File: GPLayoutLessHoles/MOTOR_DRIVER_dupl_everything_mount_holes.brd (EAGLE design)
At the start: 340.4 x 63 mm, 196 parts, among them T1 2N2222, T2 2N2222, T3 2N2222, T4 2N2222, U1 ATMEGA328P_TQFP, U7 ATMEGA328P_TQFP, Y1 16MHz, Y2 16MHz

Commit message: added more mounting holes and headers, renamed switches. ordered this 3/20
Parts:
- added H10, H11, H12, H13, H14, H15, H16, H9: MOUNT-HOLE3.3, holes:3,3
- added SV19, SV20: (no value), con-lsta:FE04-1
- moved SV16 4.50 mm to (315.0, 22.6)
- moved SV9 4.00 mm to (144.5, 22.6)
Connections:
- new net THERM1: LED1.THERMAL
- new net THERM1_DUP: LED3.THERMAL
- new net THERM2: LED2.THERMAL
- new net THERM2_DUP: LED4.THERMAL
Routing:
- net GND_TOP2: track 54.0 -> 50.3 mm
- net GND_TOP2_DUP: track 54.0 -> 50.9 mm
- net 7_4V_TOP2: track 71.2 -> 68.2 mm
- net 7_4V_TOP2_DUP: track 71.2 -> 68.3 mm
- net LED2HI_DUP: track 14.0 -> 12.7 mm
- net LED2HI: track 14.0 -> 12.7 mm
- net LED1LO_DUP: track 13.4 -> 12.2 mm
- net LED1HI_DUP: track 13.0 -> 11.9 mm
- net LED2LO_DUP: track 13.2 -> 12.1 mm
- net LED2LO: track 13.2 -> 12.1 mm
- net LED1HI: track 13.0 -> 12.0 mm
- net LED1LO: track 13.4 -> 12.4 mm
- net N$19: track 20.4 -> 19.5 mm
- net N$45: track 20.4 -> 19.5 mm
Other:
- board text added: "SENSE"
- board text added: "SW1"
- board text added: "SW2"
- board text added: "SW3"
- board text added: "SW4"

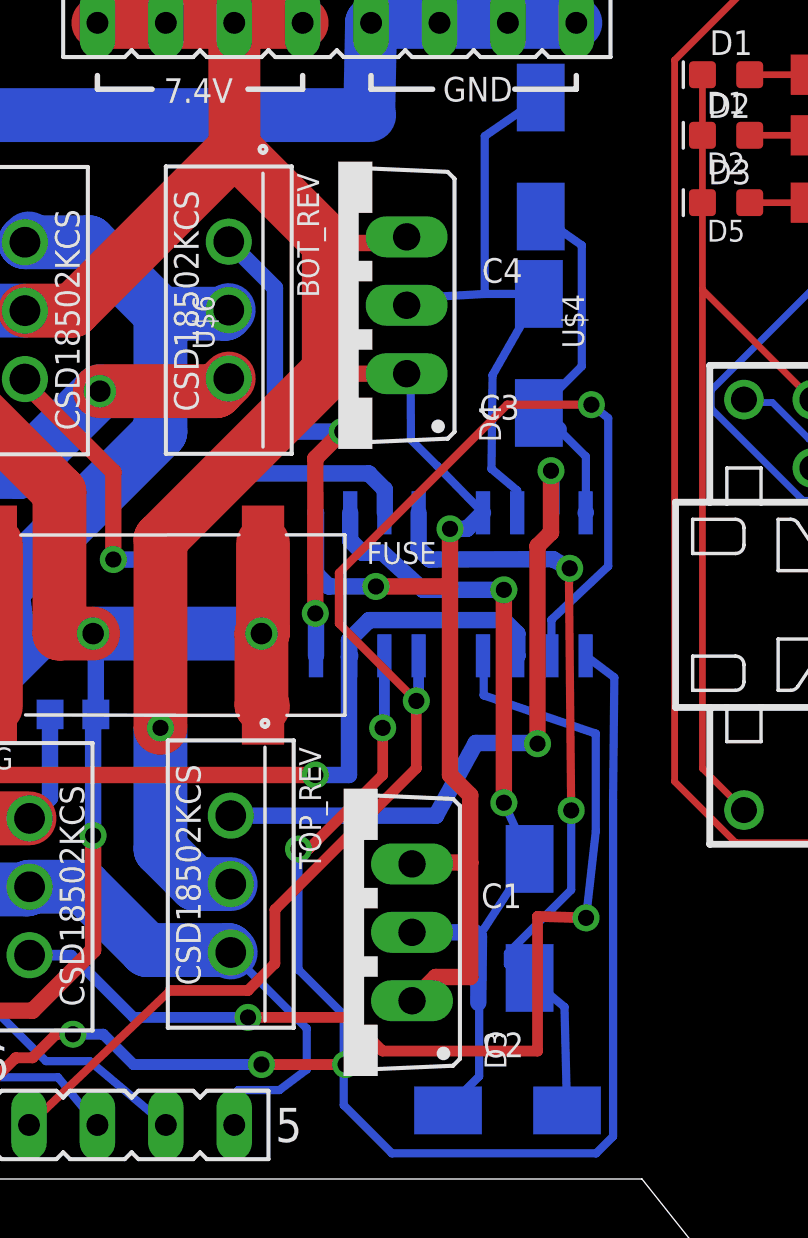
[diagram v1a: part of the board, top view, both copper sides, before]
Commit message: some modified board and new driving code for single thread and half or full bridge
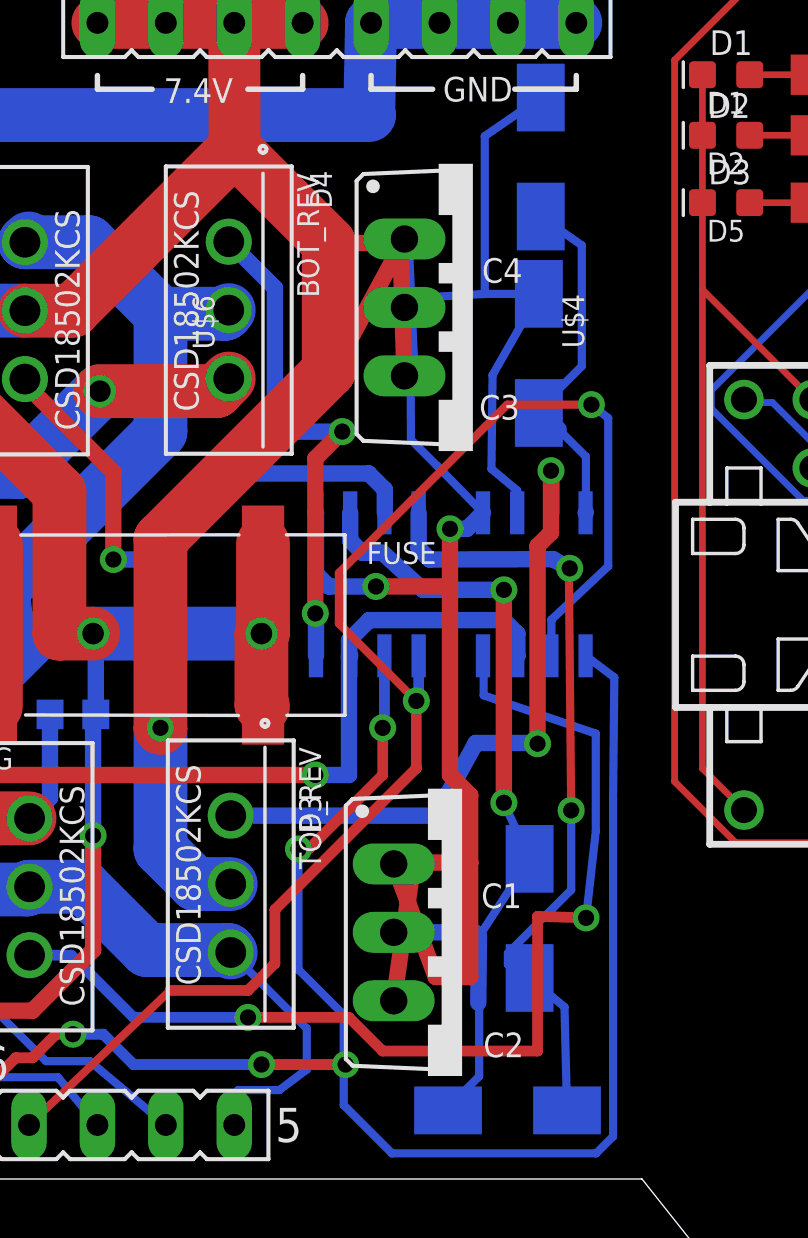
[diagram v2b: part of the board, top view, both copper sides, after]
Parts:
- R17, R35: value 10m -> 20m
- R18, R36: value 10k -> 100k
- moved D4 5.00 mm to (33.6, 32.4), turned to 270 degrees
- moved D3 4.40 mm to (33.2, 9.16), turned to 270 degrees
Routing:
- net 7_4V_TOP: track 136.8 -> 157.6 mm
- net N$5: track 30.6 -> 31.3 mm
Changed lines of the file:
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@@
 <setting verticaltext="up"/>
 </settings>
-<grid distance="0.5" unitdist="mm" unit="mm" style="lines" multiple="1" display="yes" altdistance="0.25" altunitdist="mm" altunit="mm"/>
+<grid distance="0.1" unitdist="mm" unit="mm" style="lines" multiple="1" display="yes" altdistance="0.01" altunitdist="mm" altunit="mm"/>
 <layers>
-<layer number="1" name="Top" color="4" fill="1" visible="yes" active="yes"/>
+<layer number="1" name="Top" color="4" fill="1" visible="no" active="yes"/>
 <layer number="2" name="Route2" color="1" fill="3" visible="no" active="no"/>
 <layer number="3" name="Route3" color="4" fill="3" visible="no" active="no"/>
@@
 <layer number="14" name="Route14" color="1" fill="6" visible="no" active="no"/>
 <layer number="15" name="Route15" color="4" fill="6" visible="no" active="no"/>
-<layer number="16" name="Bottom" color="1" fill="1" visible="yes" active="yes"/>
+<layer number="16" name="Bottom" color="1" fill="1" visible="no" active="yes"/>
 <layer number="17" name="Pads" color="2" fill="1" visible="yes" active="yes"/>
 <layer number="18" name="Vias" color="2" fill="1" visible="yes" active="yes"/>
@@
 <attribute name="VALUE" x="109.3604" y="15.437" size="0.8128" layer="27" ratio="10" rot="R180"/>
 </element>
-<element name="D3" library="diode" package="TO220ABS" value="BYV32" x="28.8" y="9.158" smashed="yes" rot="R90">
-<attribute name="NAME" x="34.8452" y="4.078" size="0.8128" layer="25" ratio="10" rot="R90"/>
-<attribute name="VALUE" x="36.42" y="4.078" size="0.8128" layer="27" ratio="10" rot="R90"/>
-</element>
-<element name="D4" library="diode" package="TO220ABS" value="BYV32" x="28.6" y="32.44" smashed="yes" rot="R90">
-<attribute name="NAME" x="34.6452" y="27.36" size="0.8128" layer="25" ratio="10" rot="R90"/>
-<attribute name="VALUE" x="36.22" y="27.36" size="0.8128" layer="27" ratio="10" rot="R90"/>
+<element name="D3" library="diode" package="TO220ABS" value="BYV32" x="33.2" y="9.158" smashed="yes" rot="R270">
+<attribute name="NAME" x="27.1548" y="14.238" size="0.8128" layer="25" ratio="10" rot="R270"/>
+<attribute name="VALUE" x="25.58" y="14.238" size="0.8128" layer="27" ratio="10" rot="R270"/>
+</element>
+<element name="D4" library="diode" package="TO220ABS" value="BYV32" x="33.6" y="32.36" smashed="yes" rot="R270">
+<attribute name="NAME" x="27.5548" y="37.44" size="0.8128" layer="25" ratio="10" rot="R270"/>
+<attribute name="VALUE" x="25.98" y="37.44" size="0.8128" layer="27" ratio="10" rot="R270"/>
 </element>
 <element name="MOTOR_POS" library="solpad" package="SE14" value="SE14" x="3.51" y="13.61" smashed="yes">
@@
 <attribute name="VALUE" x="70.7873" y="6.0282" size="1.27" layer="27" ratio="10"/>
 </element>
-<element name="R17" library="rcl" package="R2512" value="10m" x="14.394540625" y="18.11175" smashed="yes" rot="MR315">
+<element name="R17" library="rcl" package="R2512" value="20m" x="14.394540625" y="18.11175" smashed="yes" rot="MR315">
 <attribute name="NAME" x="14.84355625" y="21.2548375" size="0.8128" layer="26" rot="MR315"/>
 <attribute name="VALUE" x="18.43565625" y="17.662734375" size="0.8128" layer="28" rot="MR315"/>
@@
 <attribute name="VALUE" x="4.528" y="14.202" size="0.8128" layer="28" ratio="10" rot="MR0"/>
 </element>
-<element name="R18" library="rcl" package="R0603" value="10k" x="6.875" y="20.5" smashed="yes" rot="MR0">
+<element name="R18" library="rcl" package="R0603" value="100k" x="6.875" y="20.5" smashed="yes" rot="MR0">
 <attribute name="NAME" x="7.51" y="21.135" size="0.8128" layer="26" rot="MR0"/>
 <attribute name="VALUE" x="7.51" y="18.595" size="0.8128" layer="28" rot="MR0"/>
@@
 <attribute name="VALUE" x="240.7873" y="6.0282" size="1.27" layer="27" ratio="10"/>
 </element>
-<element name="R35" library="rcl" package="R2512" value="10m" x="184.394540625" y="18.11175" smashed="yes" rot="MR315">
+<element name="R35" library="rcl" package="R2512" value="20m" x="184.394540625" y="18.11175" smashed="yes" rot="MR315">
 <attribute name="NAME" x="184.84355625" y="21.2548375" size="0.8128" layer="26" rot="MR315"/>
 <attribute name="VALUE" x="188.43565625" y="17.662734375" size="0.8128" layer="28" rot="MR315"/>
@@
 <attribute name="VALUE" x="174.528" y="14.202" size="0.8128" layer="28" ratio="10" rot="MR0"/>
 </element>
-<element name="R36" library="rcl" package="R0603" value="10k" x="176.875" y="20.5" smashed="yes" rot="MR0">
+<element name="R36" library="rcl" package="R0603" value="100k" x="176.875" y="20.5" smashed="yes" rot="MR0">
 <attribute name="NAME" x="177.51" y="21.135" size="0.8128" layer="26" rot="MR0"/>
 <attribute name="VALUE" x="177.51" y="18.595" size="0.8128" layer="28" rot="MR0"/>
@@
 <wire x1="34.75" y1="21.875" x2="34.75" y2="13.97" width="0.6096" layer="1"/>
 <wire x1="34.75" y1="13.97" x2="35.7052" y2="11.8838" width="0.3048" layer="16"/>
-<wire x1="31.34" y1="9.158" x2="33.6676" y2="9.158" width="0.6096" layer="16"/>
+<wire x1="30.66" y1="9.158" x2="33.6676" y2="9.158" width="0.6096" layer="16"/>
 <wire x1="33.6676" y1="9.158" x2="33.8256" y2="9" width="0.6096" layer="16"/>
 <wire x1="31.75" y1="21.875" x2="30.25" y2="23.25" width="0.6096" layer="16"/>
@@
 <wire x1="34.04" y1="38.72" x2="36.12" y2="40.1522" width="0.3048" layer="16"/>
 <wire x1="34.04" y1="32.8596" x2="31.33" y2="32.7072" width="0.3048" layer="16"/>
-<wire x1="31.33" y1="32.7072" x2="31.14" y2="32.44" width="0.6096" layer="16"/>
+<wire x1="31.33" y1="32.7072" x2="31.06" y2="32.36" width="0.6096" layer="16"/>
 <wire x1="35.245" y1="24.7343" x2="35.245" y2="25.5626" width="0.3048" layer="16"/>
 <wire x1="35.245" y1="25.5626" x2="34.29" y2="26.3652" width="0.3048" layer="16"/>
@@
 <wire x1="32.275" y1="26.475" x2="31.3" y2="27.45" width="0.3048" layer="16"/>
 <wire x1="31.3" y1="27.45" x2="31.29" y2="29.75" width="0.3048" layer="16"/>
-<wire x1="31.29" y1="29.75" x2="31.14" y2="29.9" width="0.6096" layer="16"/>
+<wire x1="31.29" y1="29.75" x2="31.06" y2="34.9" width="0.6096" layer="16"/>
 <wire x1="27.75" y1="24.7593" x2="27.775" y2="24.7343" width="0.6096" layer="16"/>
 <via x="32.75" y="24.1404" extent="1-16" drill="0.6"/>
@@
 <wire x1="22" y1="12.25" x2="22" y2="16.75" width="2" layer="16"/>
 <wire x1="28.25" y1="34.75" x2="30.91" y2="34.75" width="0.6096" layer="1"/>
-<wire x1="30.91" y1="34.75" x2="31.14" y2="34.98" width="0.6096" layer="1"/>
-<wire x1="31.14" y1="29.9" x2="28.35" y2="29.9" width="0.6096" layer="1"/>
+<wire x1="30.91" y1="34.75" x2="31.06" y2="29.82" width="0.6096" layer="1"/>
+<wire x1="31.06" y1="34.9" x2="28.35" y2="29.9" width="0.6096" layer="1"/>
 <wire x1="28.35" y1="29.9" x2="28.25" y2="30" width="0.6096" layer="1"/>
 <wire x1="33.5" y1="11.75" x2="31.392" y2="11.75" width="0.6096" layer="1"/>
-<wire x1="31.392" y1="11.75" x2="31.34" y2="11.698" width="0.6096" layer="1"/>
+<wire x1="31.392" y1="11.75" x2="30.66" y2="6.618" width="0.6096" layer="1"/>
 <wire x1="33.5" y1="7.5" x2="32.222" y2="7.5" width="0.6096" layer="1"/>
-<wire x1="32.222" y1="7.5" x2="31.34" y2="6.618" width="0.6096" layer="1"/>
+<wire x1="32.222" y1="7.5" x2="30.66" y2="11.698" width="0.6096" layer="1"/>
 <wire x1="33.5" y1="11.75" x2="33.5" y2="7.5" width="0.6096" layer="1"/>
 <wire x1="28.25" y1="30" x2="22" y2="23.75" width="2" layer="1"/>
